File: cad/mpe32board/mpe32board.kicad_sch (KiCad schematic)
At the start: 2 parts, among them J1 Conn_ST_STDC14, U2 STM32H743VIHx

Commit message: more pcb additions + research
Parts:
- removed U2: STM32H743VIHx, Package_BGA:TFBGA-100_8x8mm_Layout10x10_P0.8mm, symbol MCU_ST_STM32H7:STM32H743VIHx
- added C1: 4.7μF, symbol Device:C_Small
- added C10, C11, C12, C13, C14, C2, C22, C23, C24, C3, C4, C5, C6, C7, C8, C9: 100nF, symbol Device:C_Small
- added C15, C16: 2.2μF, symbol Device:C_Small
- added C17, C19: 10μF, symbol Device:C_Small
- added C18, C20: 0.1μF, symbol Device:C_Small
- added C21: 1μF, symbol Device:C_Small
- added J2: USB_C_Receptacle_USB2.0_16P, symbol Connector:USB_C_Receptacle_USB2.0_16P
- added R1, R2: 10kΩ, symbol Device:R_Small
- added R3, R4: 5.1kΩ, symbol Device:R_Small
- added SW1, SW2: SW_Push, symbol Switch:SW_Push
- added U1: STM32H743IIKx, Package_BGA:UFBGA-201_10x10mm_Layout15x15_P0.65mm, symbol MCU_ST_STM32H7:STM32H743IIKx
- added U2: USBLC6-2P6, Package_TO_SOT_SMD:SOT-666, symbol Power_Protection:USBLC6-2P6
- added U3: AMS1117-3.3, Package_TO_SOT_SMD:SOT-223-3_TabPin2, symbol Regulator_Linear:AMS1117-3.3
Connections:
- net +3V3: now also C1.1, C10.1, C11.1, C12.1, C13.1, C14.1, C19.1, C2.1, C20.1, C21.1, C22.1, C23.1, C24.1, C3.1, C4.1, C5.1, C6.1, C7.1, C8.1, C9.1, R2.2, SW2.2, U1.C1 (VBAT), U1.C5 (VDD), U1.C6 (PDR_ON), U1.C7 (VDD), U1.C8 (VDD), U1.C9 (VDD), U1.F3 (VDD), U1.G13 (VDD), U1.G3 (VDD), U1.H13 (VDD33_USB), U1.J12 (VDD), U1.J13 (VDD), U1.K4 (VDD), U1.N10 (VDD), U1.N8 (VDD), U1.N9 (VDD), U1.P1 (VREF+), U1.R1 (VDDA), U3.2 (VO)
- net GND: now also C1.2, C10.2, C11.2, C12.2, C13.2, C14.2, C15.2, C16.2, C17.2, C18.2, C19.2, C2.2, C20.2, C21.2, C22.2, C23.2, C24.2, C3.2, C4.2, C5.2, C6.2, C7.2, C8.2, C9.2, J2.A1 (GND), J2.A12 (GND), J2.B1 (GND), J2.B12 (GND), J2.S1 (SHIELD), R1.2, R3.2, R4.2, SW1.2, U1.D5 (VSS), U1.D7 (VSS), U1.D8 (VSS), U1.D9 (VSS), U1.F10 (VSS), U1.F12 (VSS), U1.F2 (VSS), U1.F6 (VSS), U1.F7 (VSS), U1.F8 (VSS), U1.F9 (VSS), U1.G10 (VSS), U1.G12 (VSS), U1.G2 (VSS), U1.G6 (VSS), U1.G7 (VSS), U1.G8 (VSS), U1.G9 (VSS), U1.H10 (VSS), U1.H12 (VSS), U1.H6 (VSS), U1.H7 (VSS), U1.H8 (VSS), U1.H9 (VSS), U1.J10 (VSS), U1.J6 (VSS), U1.J7 (VSS), U1.J8 (VSS), U1.J9 (VSS), U1.K10 (VSS), U1.K6 (VSS), U1.K7 (VSS), U1.K8 (VSS), U1.K9 (VSS), U1.L4 (VSS), U1.M1 (VSSA), U1.M8 (VSS), U1.M9 (VSS), U1.N1 (VREF-), U2.2 (GND), U3.1 (GND)
- net JTDI: now also U1.A13 (PA15)
- net LPUART1_RX: now also U1.D15 (PA10)
- net LPUART1_TX: now also U1.E15 (PA9)
- net NRST: now also R2.1, SW1.1, U1.J1 (NRST)
- net SWCLK: now also U1.A14 (PA14)
- net SWDIO: now also U1.A15 (PA13)
- net SWO: now also U1.A10 (PB3)
- new net: C16.1, U1.M10 (VCAP)
- new net: J2.B5 (CC2), R4.1
- new net: J2.A7 (D-), J2.B7 (D-), U2.1 (I/O1)
- new net: J2.A6 (D+), J2.B6 (D+), U2.3 (I/O2)
- new net: J2.A5 (CC1), R3.1
- new net: C15.1, U1.F13 (VCAP)
- new net +5V: C17.1, C18.1, J2.A4 (VBUS), J2.A9 (VBUS), J2.B4 (VBUS), J2.B9 (VBUS), U2.5 (VBUS), U3.3 (VI)
- new net BOOT0: R1.1, SW2.1, U1.D6 (BOOT0)
- new net OTG_FS_DM: U1.C15 (PA11), U2.6 (I/O1)
- new net OTG_FS_DP: U1.B15 (PA12), U2.4 (I/O2)
- no-connect marks 1 -> 3
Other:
- note added: "decoupling capacitors"
- note added: "extra for vdd"
- note added: "for all the vdd"
- note added: "https://www.reddit.com/r/PrintedCircuitBoard/comments/1keinxe/comment/mqk7sqr"
- note added: "ldo 3v3"
- note added: "low esr?"
- note added: "optional 100nF + 1x1μF"
- note added: "pull high > boot"
- note added: "pull low > reset"
- note added: "reset and boot buttons"
- note added: "stlink-jtag/swd for debug and programming"
- note added: "usb-c power and data"
- note added: "usbvdd"
- note removed: "stlink-jtag/swd"
- moved on the sheet: J1

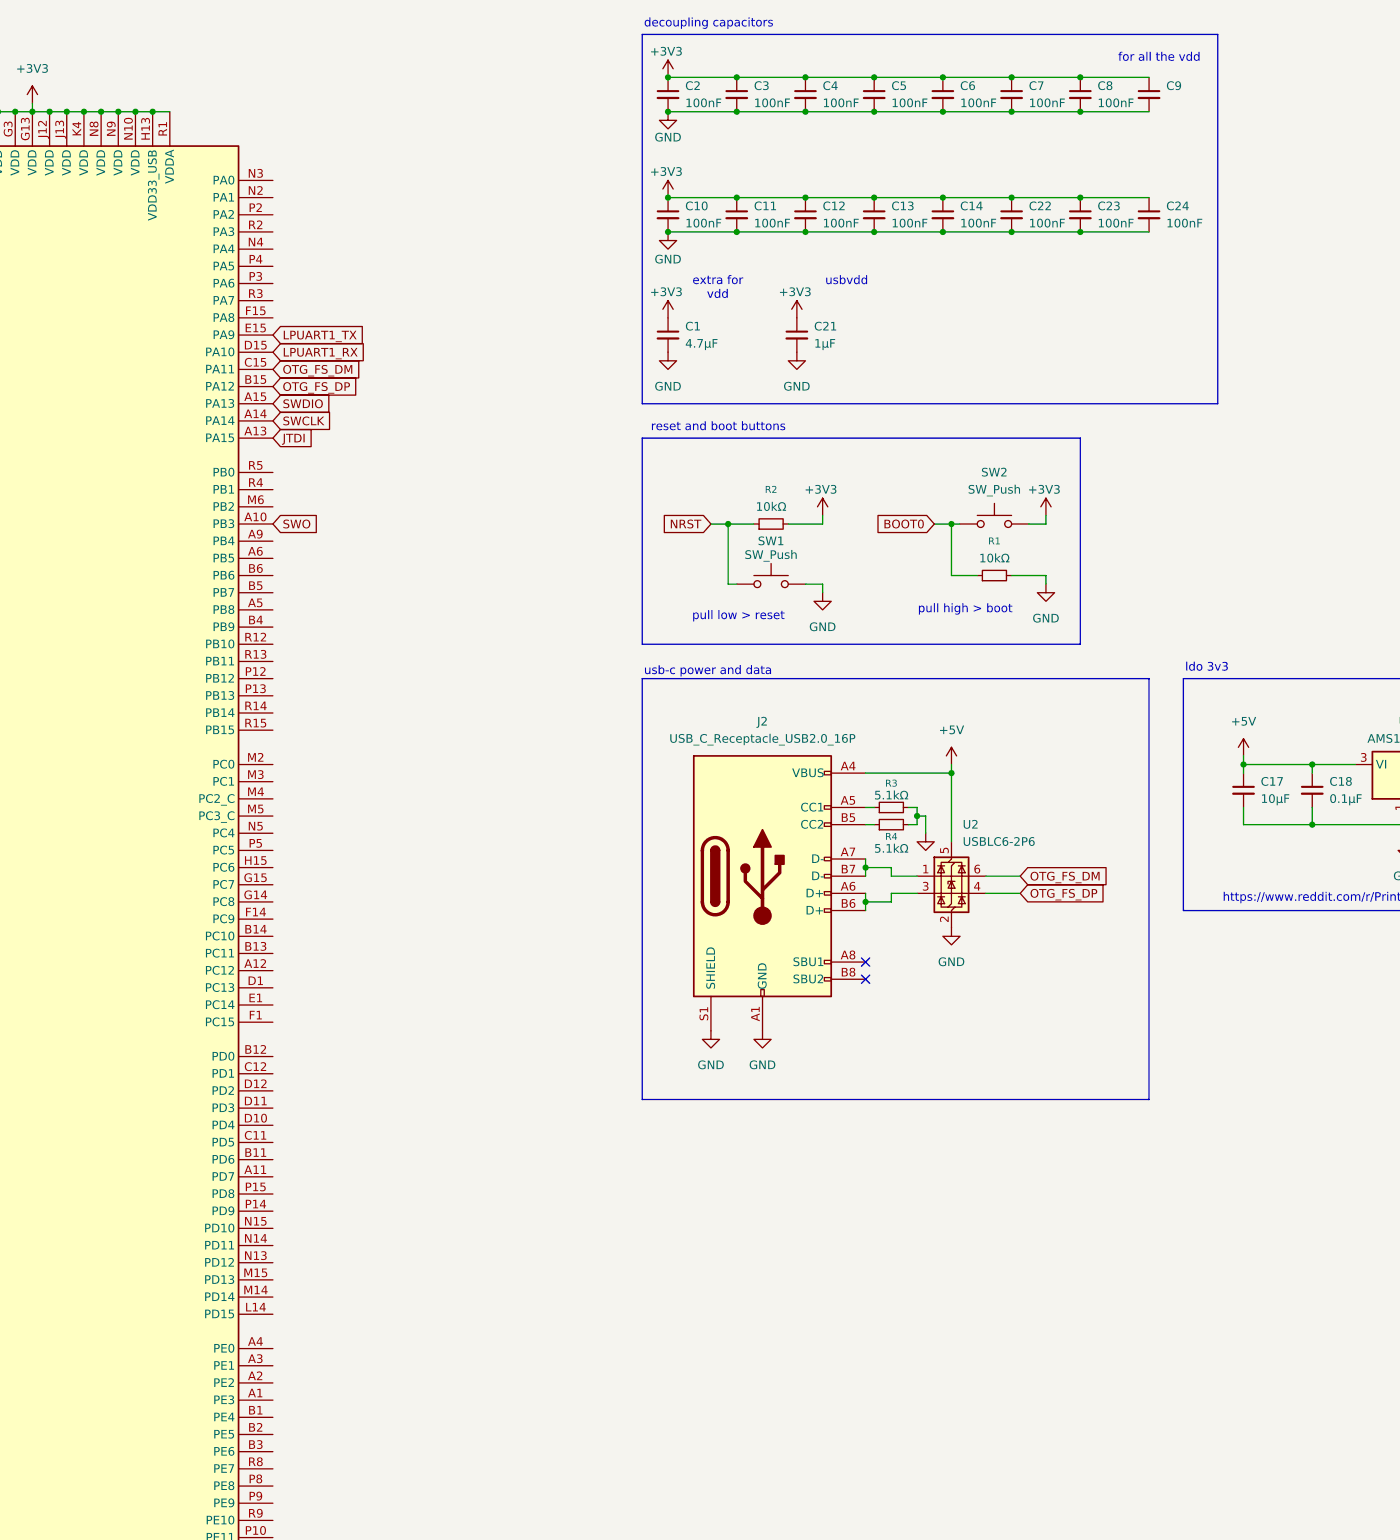
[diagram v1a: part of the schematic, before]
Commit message: pcb i2c mux + connectors
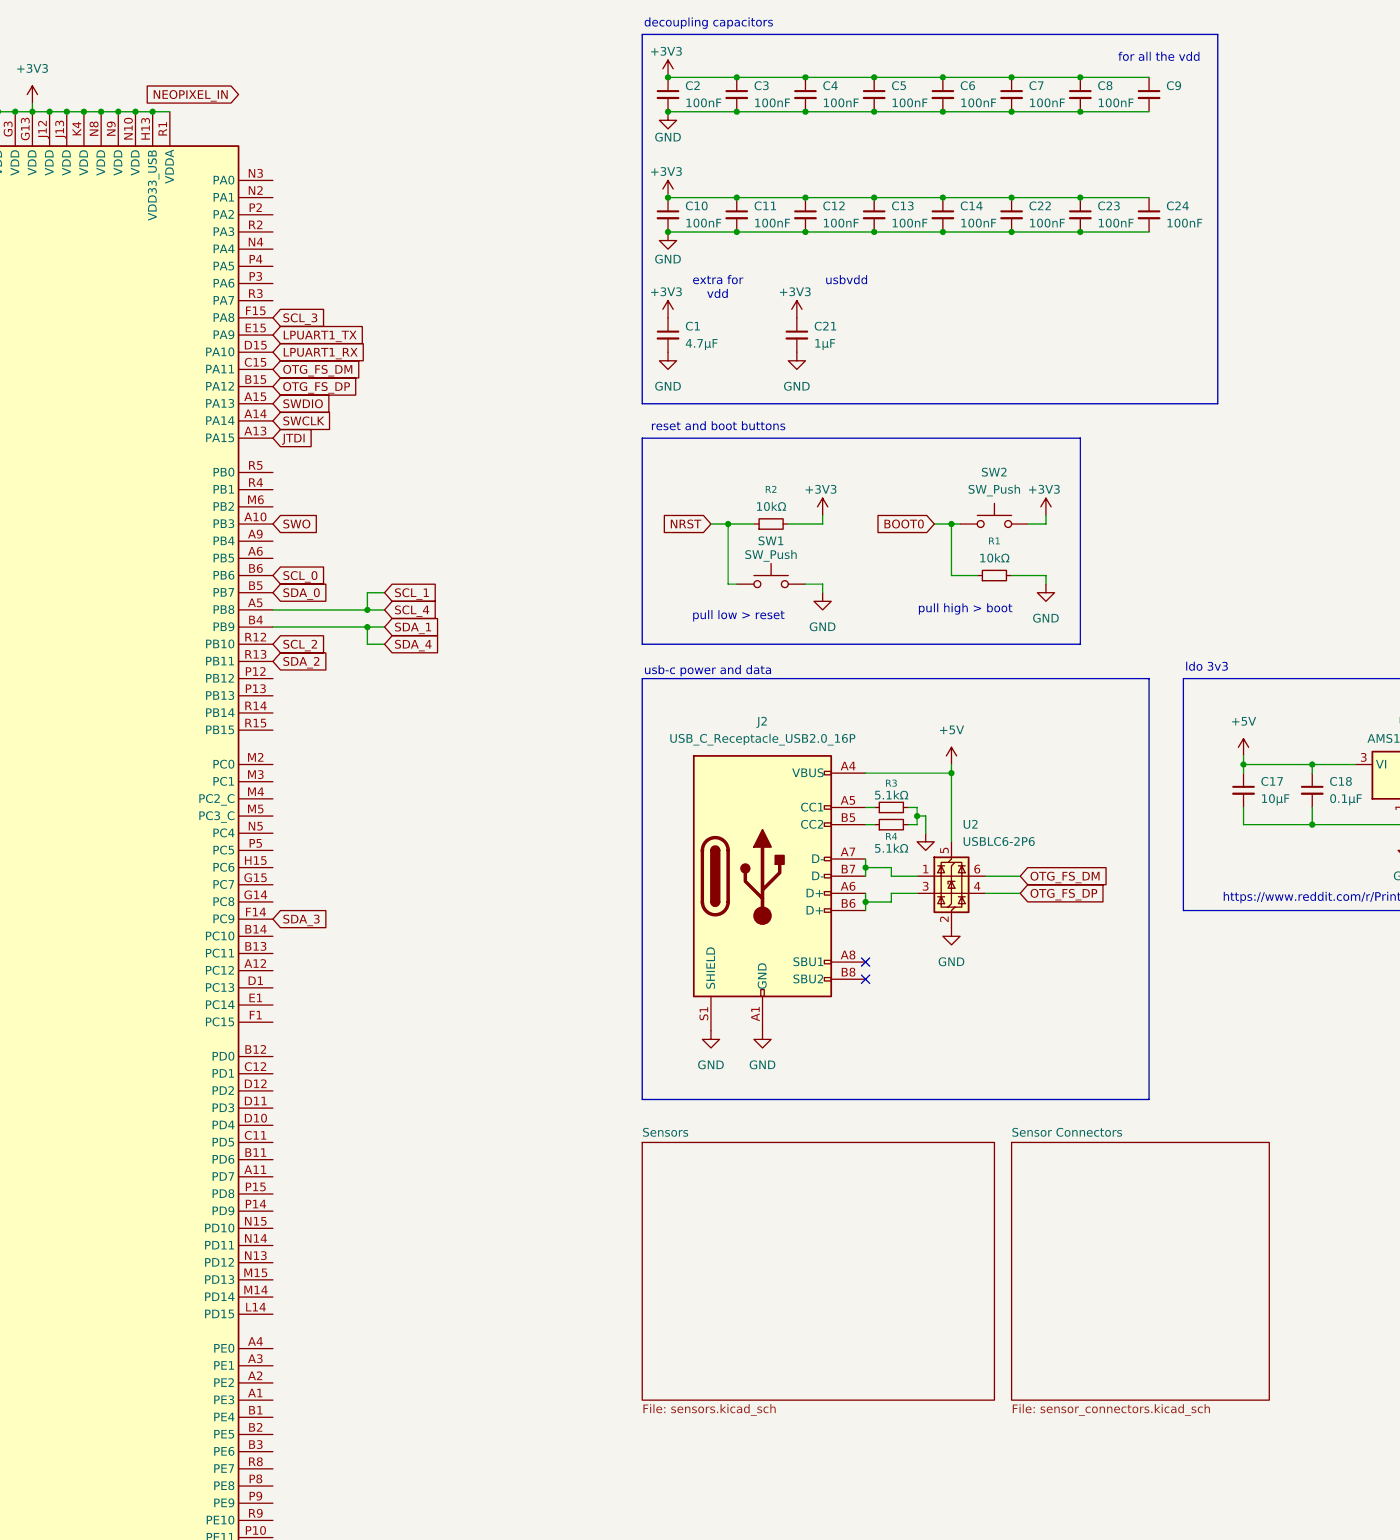
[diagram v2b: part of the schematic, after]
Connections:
- net SCL_1: now reaches U1.A5 (PB8)
- net SDA_1: now reaches U1.B4 (PB9)
- net SDA_0: now reaches U1.B5 (PB7)
- net SCL_0: now reaches U1.B6 (PB6)
- net SDA_3: now reaches U1.F14 (PC9)
- net SCL_3: now reaches U1.F15 (PA8)
- net SCL_2: now reaches U1.R12 (PB10)
- net SDA_2: now reaches U1.R13 (PB11)
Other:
- added sheet Sensor Connectors (sensor_connectors.kicad_sch)
- added sheet Sensors (sensors.kicad_sch)

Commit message: add sdram
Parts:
- removed U1: STM32H743IIKx, Package_BGA:UFBGA-201_10x10mm_Layout15x15_P0.65mm, symbol MCU_ST_STM32H7:STM32H743IIKx
- added C25: 100nF, symbol Device:C_Small
- added U10: W9812G6KH-75, Package_SO:TSOP-II-54_22.2x10.16mm_P0.8mm, symbol Memory_RAM:W9812G6KH-75
- added U9: STM32H743IITx, Package_QFP:LQFP-176_24x24mm_P0.5mm, symbol MCU_ST_STM32H7:STM32H743IITx
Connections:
- net +3V3: now also C25.1, U10.1 (VDD), U10.14 (VDD), U10.27 (VDD), U10.3 (VDDQ), U10.43 (VDDQ), U10.49 (VDDQ), U10.9 (VDDQ), U9.103 (VDD), U9.114 (VDD33_USB), U9.127 (VDD), U9.136 (VDD), U9.149 (VDD), U9.15 (VDD), U9.159 (VDD), U9.172 (VDD), U9.23 (VDD), U9.36 (VDD), U9.38 (VREF+), U9.39 (VDDA), U9.49 (VDD), U9.6 (VBAT), U9.62 (VDD), U9.72 (VDD), U9.82 (VDD), U9.91 (VDD)
- net BOOT0: now also U9.166 (BOOT0)
- net GND: now also C25.2, U10.12 (VSSQ), U10.28 (VSS), U10.41 (VSS), U10.46 (VSSQ), U10.52 (VSSQ), U10.54 (VSS), U10.6 (VSSQ), U9.102 (VSS), U9.113 (VSS), U9.126 (VSS), U9.135 (VSS), U9.14 (VSS), U9.148 (VSS), U9.158 (VSS), U9.171 (PDR_ON), U9.22 (VSS), U9.37 (VSSA), U9.48 (VSS), U9.61 (VSS), U9.71 (VSS), U9.90 (VSS)
- net JTDI: now also U9.138 (PA15)
- net LPUART1_RX: now also U9.121 (PA10)
- net LPUART1_TX: now also U9.120 (PA9)
- net NRST: now also U9.31 (NRST)
- net OTG_FS_DM: now also U9.122 (PA11)
- net OTG_FS_DP: now also U9.123 (PA12)
- net SCL_0: now also U9.164 (PB6)
- net SCL_1: now also U9.167 (PB8)
- net SCL_2: now also U9.79 (PB10)
- net SCL_3: now also U9.119 (PA8)
- net SDA_0: now also U9.165 (PB7)
- net SDA_1: now also U9.168 (PB9)
- net SDA_2: now also U9.80 (PB11)
- net SDA_3: now also U9.118 (PC9)
- net SWCLK: now also U9.137 (PA14)
- net SWDIO: now also U9.124 (PA13)
- net SWO: now also U9.161 (PB3)
- net at C16.1: now also U9.125 (VCAP)
- net at C15.1: now also U9.81 (VCAP)
- new net FMC_A0: U10.23 (A0), U9.16 (PF0)
- new net FMC_A1: U10.24 (A1), U9.17 (PF1)
- new net FMC_A10: U10.22 (A10/AP), U9.66 (PG0)
- new net FMC_A11: U10.35 (A11), U9.67 (PG1)
- new net FMC_A2: U10.25 (A2), U9.18 (PF2)
- new net FMC_A3: U10.26 (A3), U9.19 (PF3)
- new net FMC_A4: U10.29 (A4), U9.20 (PF4)
- new net FMC_A5: U10.30 (A5), U9.21 (PF5)
- new net FMC_A6: U10.31 (A6), U9.60 (PF12)
- new net FMC_A7: U10.32 (A7), U9.63 (PF13)
- new net FMC_A8: U10.33 (A8), U9.64 (PF14)
- new net FMC_A9: U10.34 (A9), U9.65 (PF15)
- new net FMC_BA0: U10.20 (BS0), U9.108 (PG4)
- new net FMC_BA1: U10.21 (BS1), U9.109 (PG5)
- new net FMC_D0: U10.2 (DQ0), U9.104 (PD14)
- new net FMC_D1: U10.4 (DQ1), U9.105 (PD15)
- new net FMC_D10: U10.45 (DQ10), U9.76 (PE13)
- new net FMC_D11: U10.47 (DQ11), U9.77 (PE14)
- new net FMC_D12: U10.48 (DQ12), U9.78 (PE15)
- new net FMC_D13: U10.50 (DQ13), U9.96 (PD8)
- new net FMC_D14: U10.51 (DQ14), U9.97 (PD9)
- new net FMC_D15: U10.53 (DQ15), U9.98 (PD10)
- new net FMC_D2: U10.5 (DQ2), U9.142 (PD0)
- new net FMC_D3: U10.7 (DQ3), U9.143 (PD1)
- new net FMC_D4: U10.8 (DQ4), U9.68 (PE7)
- new net FMC_D5: U10.10 (DQ5), U9.69 (PE8)
- new net FMC_D6: U10.11 (DQ6), U9.70 (PE9)
- new net FMC_D7: U10.13 (DQ7), U9.73 (PE10)
- new net FMC_D8: U10.42 (DQ8), U9.74 (PE11)
- new net FMC_D9: U10.44 (DQ9), U9.75 (PE12)
- new net FMC_NBL0: U10.15 (LDQM), U9.169 (PE0)
- new net FMC_NBL1: U10.39 (UDQM), U9.170 (PE1)
- new net FMC_SDCKE0: U10.37 (CKE), U9.35 (PC3_C)
- new net FMC_SDCLK: U10.38 (CLK), U9.112 (PG8)
- new net FMC_SDNCAS: U10.17 (~{CAS}), U9.160 (PG15)
- new net FMC_SDNE0: U10.19 (~{CS}), U9.34 (PC2_C)
- new net FMC_SDNRAS: U10.18 (~{RAS}), U9.59 (PF11)
- new net FMC_SDNWE: U10.16 (~{WE}), U9.32 (PC0)
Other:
- note added: "can switch between IIK and IIT"
- note added: "have a higher quality ldo!!!!"
- note added: "https://github.com/dkm1978/STM32H7IIT6-Core-board"
- note added: "sdram specs - 16 bit addresses 64-512mb any >=133mhz"
- moved on the sheet: C1, C10, C11, C12, C13, C14, C17, C18, C19, C2, C20, C21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
